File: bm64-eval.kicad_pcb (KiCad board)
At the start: 2 copper layers, 85 x 65 mm, 52 parts, among them J1 BATTERY, J2 USB, J3 HEADPHONE, J4 MIC, J5 EXT_1, J6 EXT_2, J7 EXT_3, J8 EXT_5, J9 EXT_4, SW1 RESET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

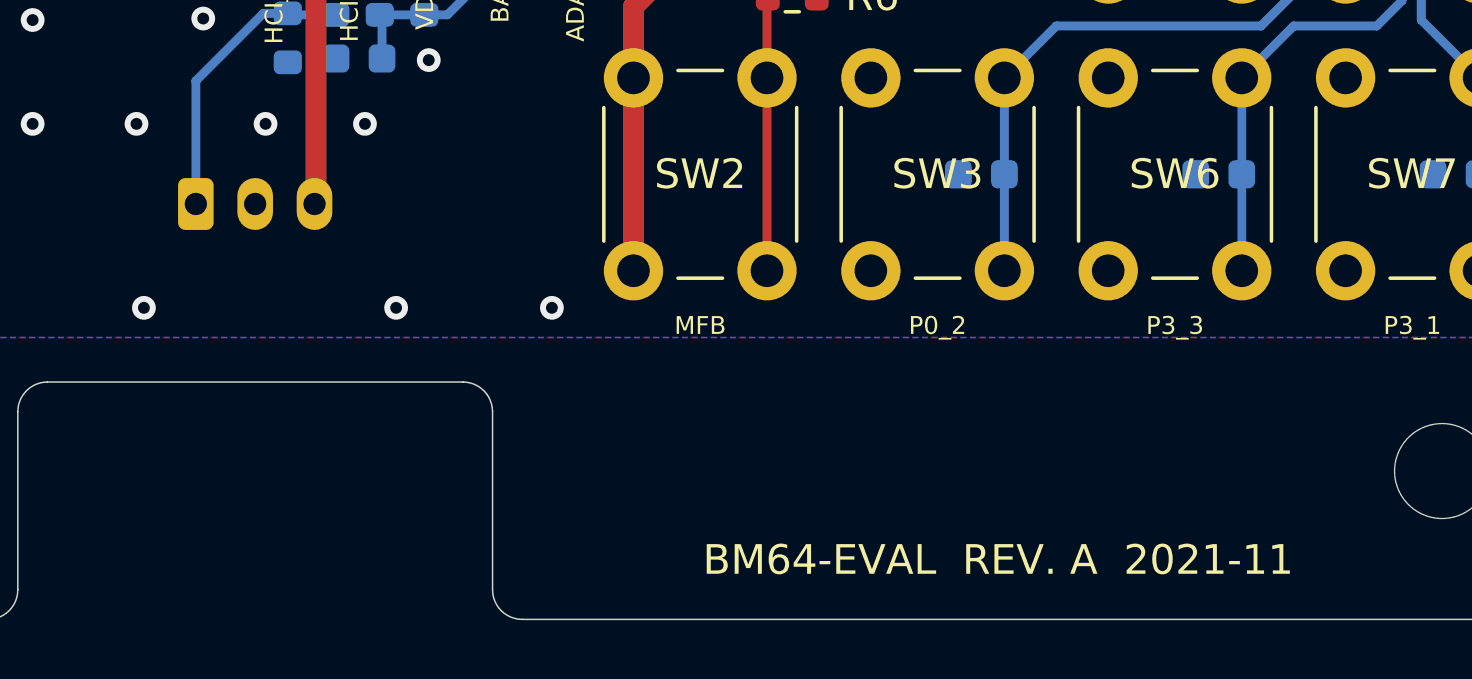
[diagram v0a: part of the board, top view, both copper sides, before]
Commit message: apply gerber settings
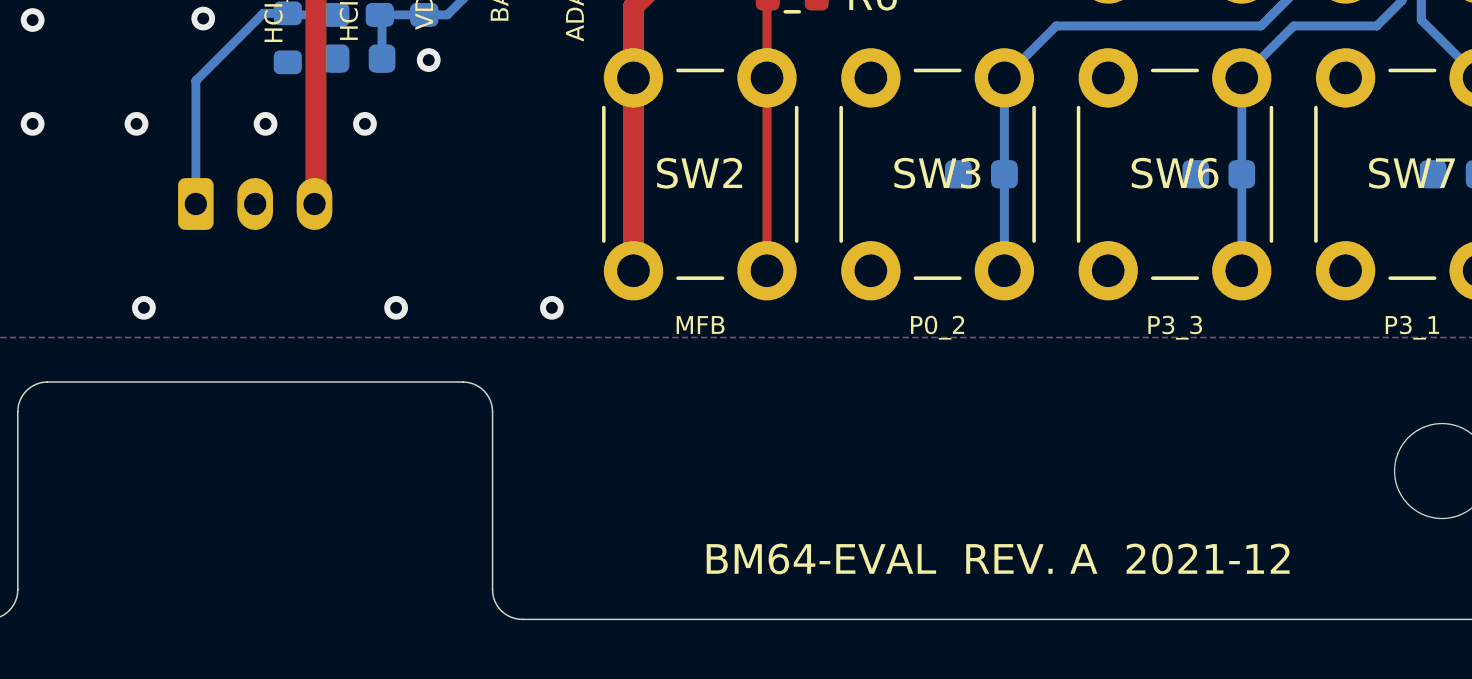
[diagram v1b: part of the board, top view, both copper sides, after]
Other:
- board text added: "BM64-EVAL REV. A 2021-12"
- board text removed: "BM64-EVAL REV. A 2021-11"

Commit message: swap R4 R5 value
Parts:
- R4: value 10M -> 7.5M
- R5: value 7.5M -> 10M
